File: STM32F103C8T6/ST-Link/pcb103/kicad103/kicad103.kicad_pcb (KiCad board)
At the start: 4 copper layers, 28 parts, among them IC1 LD1117DT33TR, J1 0480372200, J2 Conn_01x02_Socket, J3 Conn_02x05_Odd_Even, J4 Conn_01x03_Pin, J5 Conn_01x16_Pin, J6 Conn_01x16_Pin, J7 Conn_01x04_Pin, J8 Conn_01x05_Socket, U1 STM32F103C8T6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

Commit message: SWD 220R
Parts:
- added R6: 220, Resistor_SMD:R_1206_3216Metric, F.Cu at (233.1, 87.4)
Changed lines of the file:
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@@
+    )
+  )
+  (footprint "Resistor_SMD:R_1206_3216Metric" (layer "F.Cu")
+    (at 233.1375 87.4)
+    (descr "Resistor SMD 1206 (3216 Metric), square (rectangular) end terminal, IPC_7351 nominal, (Body size source: IPC-SM-782 page 72, https://www.pcb-3d.com/wordpress/wp-content/uploads/ipc-sm-782a_amendment_1_and_2.pdf), generated with kicad-footprint-generator")
+    (tags "resistor")
+    (property "Sheetfile" "kicad103.kicad_sch")
+    (property "Sheetname" "")
+    (property "ki_description" "Resistor")
+    (property "ki_keywords" "R res resistor")
+    (attr smd)
+    (fp_text reference "R6" (at 0 -1.82) (layer "F.SilkS")
+        (effects (font (size 1 1) (thickness 0.15)))
+    )
+    (fp_text value "220" (at 0 1.82) (layer "F.Fab")
+        (effects (font (size 1 1) (thickness 0.15)))
+    )
+    (fp_text user "${REFERENCE}" (at 0 0) (layer "F.Fab")
+        (effects (font (size 0.8 0.8) (thickness 0.12)))
+    )
+    (fp_line (start -0.727064 -0.91) (end 0.727064 -0.91)
+      (stroke (width 0.12) (type solid)) (layer "F.SilkS"))
+    (fp_line (start -0.727064 0.91) (end 0.727064 0.91)
+      (stroke (width 0.12) (type solid)) (layer "F.SilkS"))
+    (fp_line (start -2.28 -1.12) (end 2.28 -1.12)
+      (stroke (width 0.05) (type solid)) (layer "F.CrtYd"))
+    (fp_line (start -2.28 1.12) (end -2.28 -1.12)
+      (stroke (width 0.05) (type solid)) (layer "F.CrtYd"))
+    (fp_line (start 2.28 -1.12) (end 2.28 1.12)
+      (stroke (width 0.05) (type solid)) (layer "F.CrtYd"))
+    (fp_line (start 2.28 1.12) (end -2.28 1.12)
+      (stroke (width 0.05) (type solid)) (layer "F.CrtYd"))
+    (fp_line (start -1.6 -0.8) (end 1.6 -0.8)
+      (stroke (width 0.1) (type solid)) (layer "F.Fab"))
+    (fp_line (start -1.6 0.8) (end -1.6 -0.8)
+      (stroke (width 0.1) (type solid)) (layer "F.Fab"))
+    (fp_line (start 1.6 -0.8) (end 1.6 0.8)
+      (stroke (width 0.1) (type solid)) (layer "F.Fab"))
+    (fp_line (start 1.6 0.8) (end -1.6 0.8)
+      (stroke (width 0.1) (type solid)) (layer "F.Fab"))
+    (pad "1" smd roundrect (at -1.4625 0) (size 1.125 1.75) (layers "F.Cu" "F.Paste" "F.Mask") (roundrect_rratio 0.222222)
+      (net 22 "PB14") (pintype "passive"))
+    (pad "2" smd roundrect (at 1.4625 0) (size 1.125 1.75) (layers "F.Cu" "F.Paste" "F.Mask") (roundrect_rratio 0.222222)
+      (net 24 "PB12") (pintype "passive"))
+    (model "${KICAD6_3DMODEL_DIR}/Resistor_SMD.3dshapes/R_1206_3216Metric.wrl"
+      (offset (xyz 0 0 0))
+      (scale (xyz 1 1 1))
+      (rotate (xyz 0 0 0))
     )
   )

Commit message: Mounting holes
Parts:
- removed J4: Conn_01x03_Pin, Connector_PinHeader_2.54mm:PinHeader_1x03_P2.54mm_Vertical
- removed J6: Conn_01x16_Pin, Connector_PinHeader_2.54mm:PinHeader_1x16_P2.54mm_Vertical
- added H1: MountingHole_Pad, MountingHole:MountingHole_4.3mm_M4_Pad_Via, F.Cu at (243.2, 49.4)
- added H2: MountingHole_Pad, MountingHole:MountingHole_4.3mm_M4_Pad_Via, F.Cu at (243.2, 59.6)
- added H3: MountingHole_Pad, MountingHole:MountingHole_4.3mm_M4_Pad_Via, F.Cu at (243.2, 69.7)
- added H4: MountingHole_Pad, MountingHole:MountingHole_4.3mm_M4_Pad_Via, F.Cu at (243.2, 79.9)
- added J9: Conn_01x17_Pin, Connector_PinHeader_2.54mm:PinHeader_1x17_P2.54mm_Vertical, F.Cu at (235.8, 46.7)
- moved R2 31.8 mm to (183.5, 51.2)
- moved R1 31.8 mm to (183.5, 48.2)
- moved R5 31.8 mm to (144.4, 75.5)
- moved C5 31.8 mm to (149.4, 51.4)
- moved C6 31.8 mm to (149.4, 54.8)
- moved D2 31.8 mm to (193.8, 62.0)
- moved J3 31.8 mm to (147.0, 69.8)
- moved R4 31.8 mm to (165.1, 59.3)
- moved R6 31.8 mm to (201.7, 83.0)
- moved C1 31.8 mm to (203.4, 52.9)
- moved C2 31.8 mm to (202.8, 56.1)
- moved C3 31.8 mm to (149.4, 44.7)
- moved C4 31.8 mm to (149.4, 48.1)
- moved C7 31.8 mm to (149.4, 58.1)
- moved C8 31.8 mm to (156.0, 69.8)
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
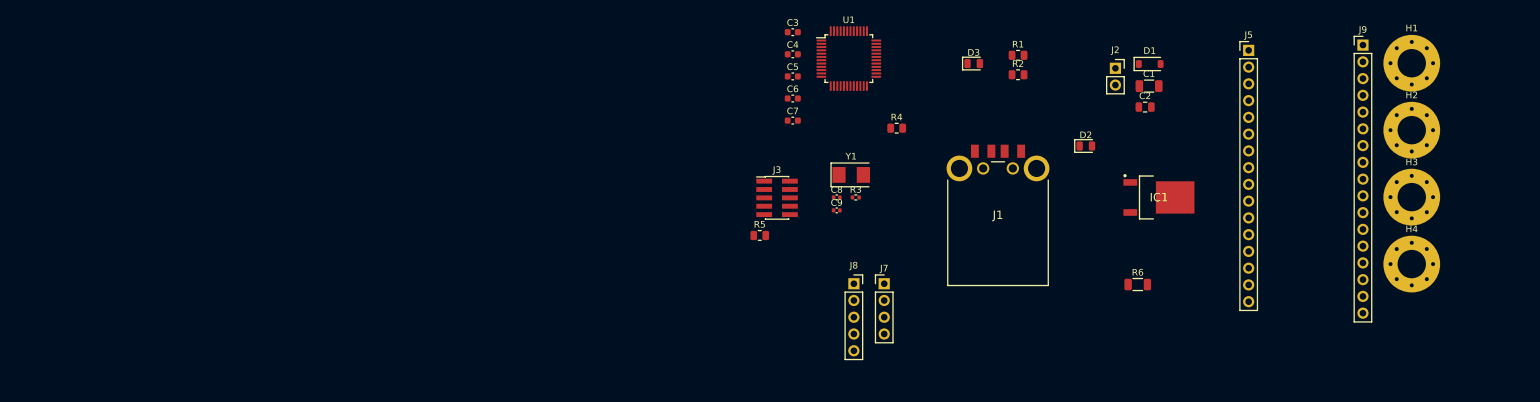
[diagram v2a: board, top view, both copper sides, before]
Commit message: Fix power lines
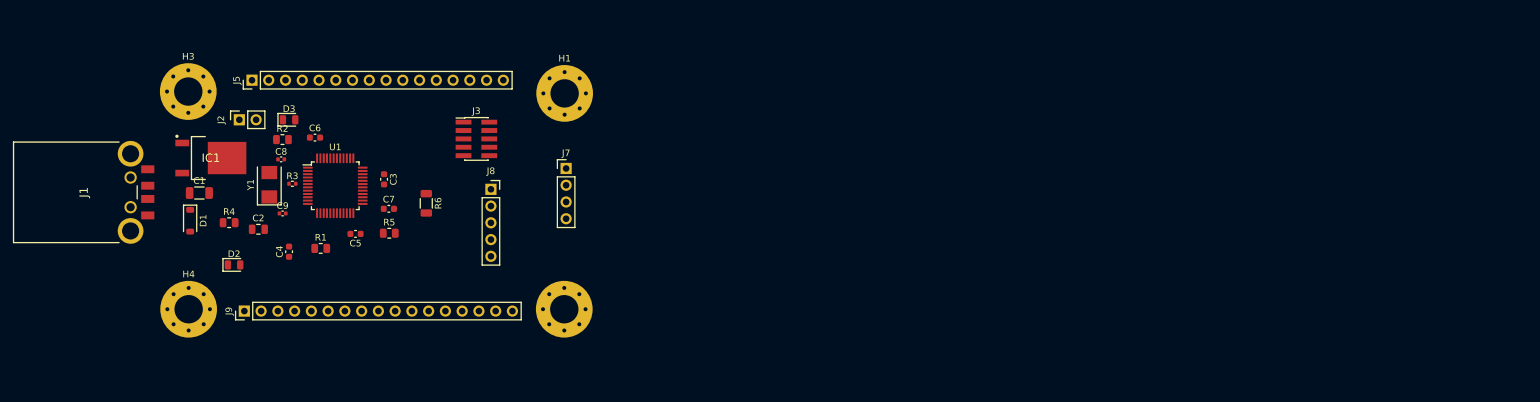
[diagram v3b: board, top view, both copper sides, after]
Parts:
- moved H3 186.2 mm to (57.7, 53.7)
- moved H4 185.6 mm to (57.8, 86.7)
- moved J9 174.3 mm to (66.2, 87.0), turned to 90 degrees
- moved J5 151.2 mm to (67.4, 52.0), turned to 90 degrees
- moved D1 147.4 mm to (58.0, 73.3), turned to -90 degrees
- moved C1 144.9 mm to (59.4, 69.1)
- moved IC1 143.8 mm to (61.1, 63.8)
- moved J1 139.1 mm to (41.4, 69.0), turned to -90 degrees
- moved C2 135.7 mm to (68.3, 74.6)
- moved J2 133.0 mm to (65.5, 58.0), turned to 90 degrees
- moved H2 131.3 mm to (114.7, 86.7)
- moved D2 130.4 mm to (64.7, 80.0)
- moved H1 128.5 mm to (114.8, 54.0)
- moved R2 111.9 mm to (72.0, 61.0)
- moved R1 109.7 mm to (77.8, 77.5)
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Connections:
- net +5V renamed Net-(D1-A)
- C2 pad 1: /3.3V -> +3.3V
- D2 pad 1: +3.3V -> Net-(D2-K)
- D2 pad 2: /3.3V -> +3.3V
- IC1 pad 4: /3.3V -> +3.3V
- R1 pad 1: +3.3V -> Net-(D2-K)
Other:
- rule pad_to_mask_clearance: 0 -> 0.038

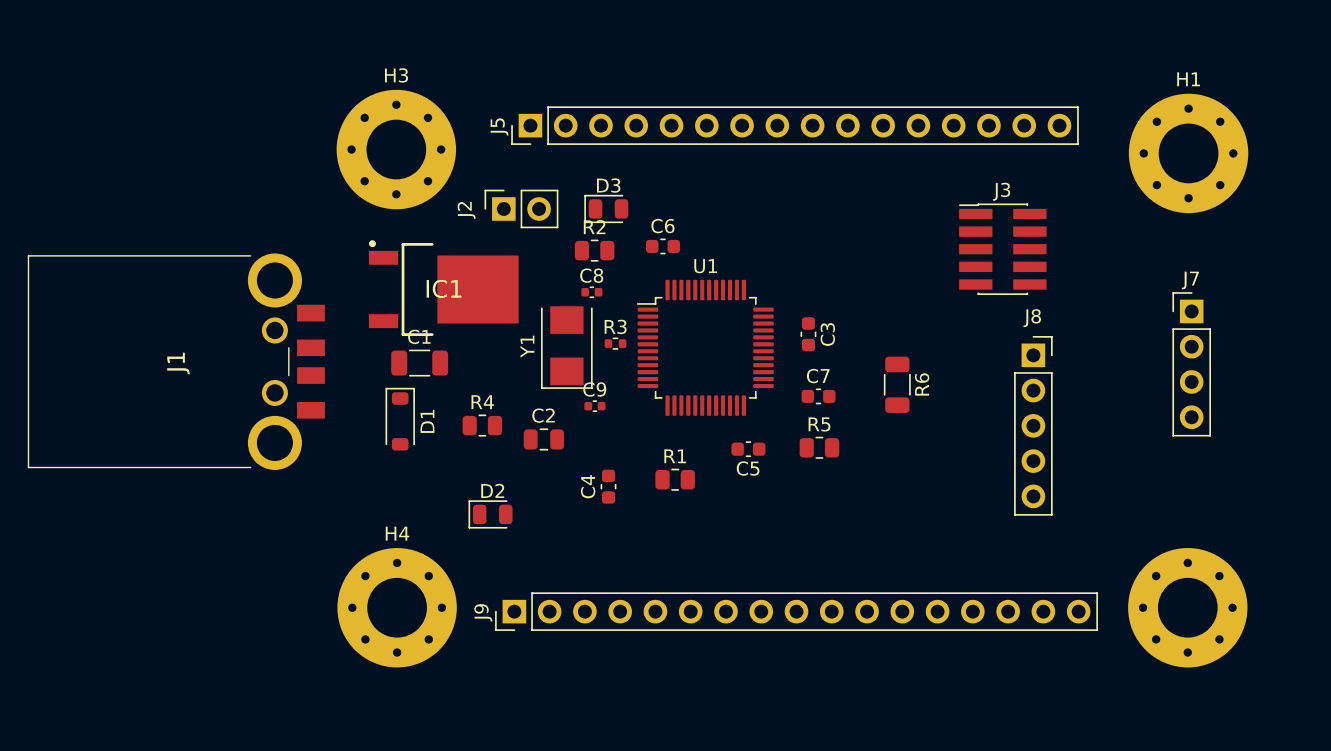
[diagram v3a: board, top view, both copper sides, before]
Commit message: USB differential pair
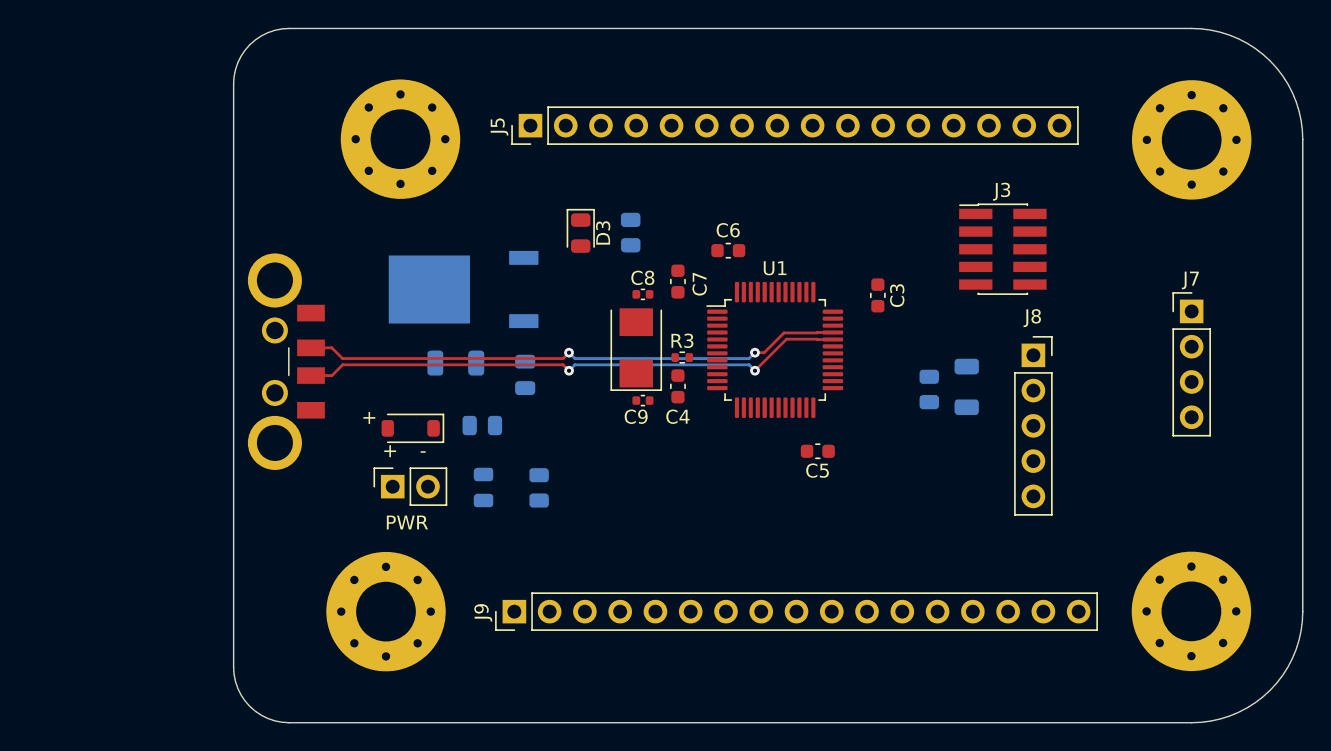
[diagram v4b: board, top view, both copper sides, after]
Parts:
- C1, C2, D2, IC1, R1, R2, R4, R5, R6: moved to B.Cu
- moved J2 21.5 mm to (57.5, 78.0)
- moved C7 13.1 mm to (78.0, 63.2), turned to 90 degrees
- moved R1 9.82 mm to (68.0, 78.1), turned to 90 degrees
- moved R5 8.96 mm to (96.1, 71.0), turned to 90 degrees
- moved C4 8.79 mm to (78.0, 70.8), turned to -90 degrees
- moved C3 5.73 mm to (92.4, 64.2)
- moved C5 5.00 mm to (88.1, 75.5)
- moved R6 5.00 mm to (98.8, 70.8)
- moved U1 5.00 mm to (85.0, 68.2)
- moved Y1 5.00 mm to (75.0, 68.0)
- moved R3 4.91 mm to (78.3, 68.7)
- moved C2 4.84 mm to (67.0, 70.0), turned to -90 degrees
- moved C6 4.71 mm to (81.6, 61.0)
- moved C8 3.68 mm to (75.5, 64.2), turned to 180 degrees
- moved C9 3.48 mm to (75.5, 71.8), turned to 180 degrees
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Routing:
- net /USB_D-: track 0.00 -> 39.4 mm, vias 0 -> 2
- net /USB_D+: track 0.00 -> 39.0 mm, vias 0 -> 2
- added copper zone on In2.Cu, net +3.3V
- added copper zone on In1.Cu, net GND
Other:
- board outline added: 77 x 50 mm
- board text added: "+"
- board text added: "-"
- board text added: "PWR"

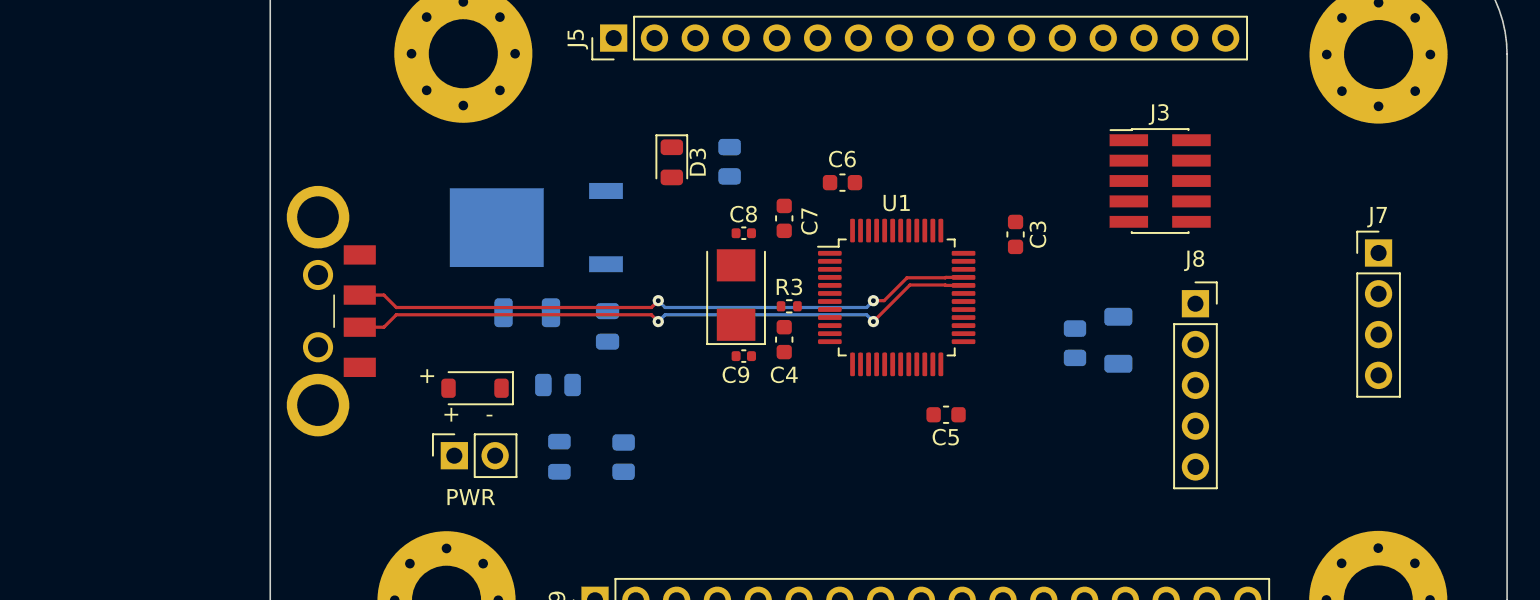
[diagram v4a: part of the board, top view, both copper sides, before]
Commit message: Connect Debug
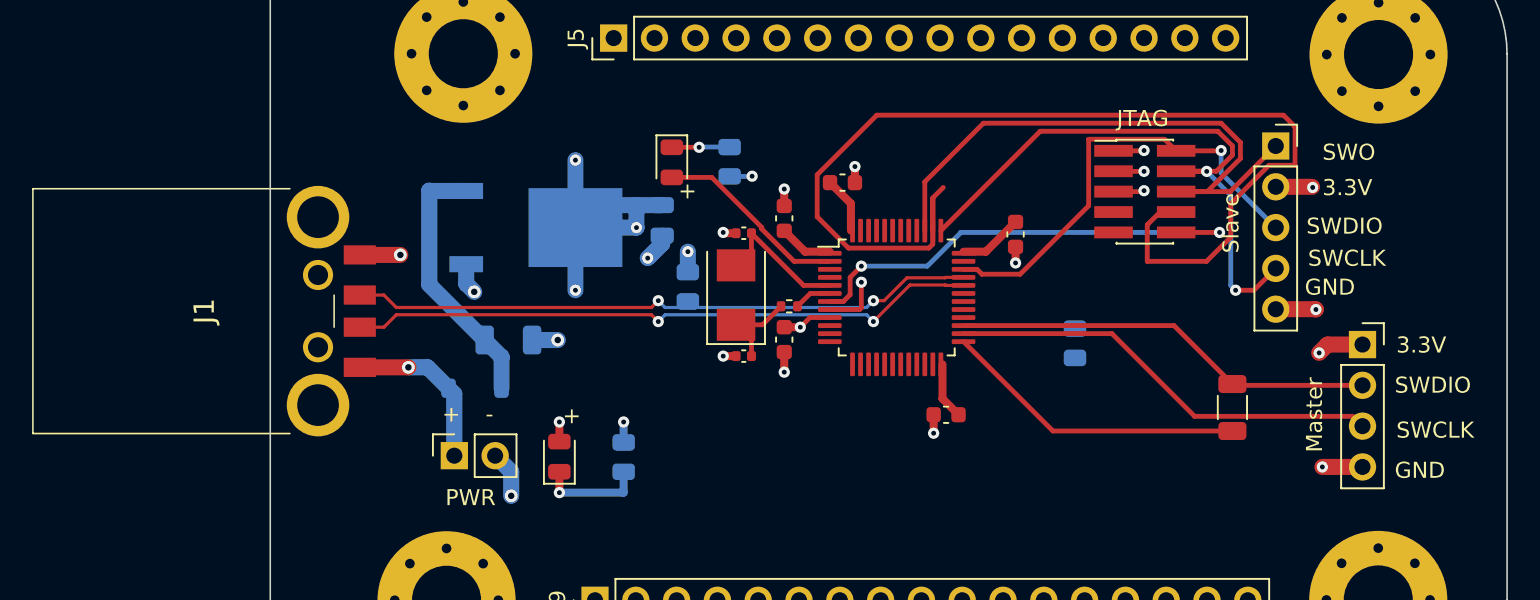
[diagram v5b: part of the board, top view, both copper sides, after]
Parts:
- D1: moved to B.Cu
- D2, R6: moved to F.Cu
- J7: footprint Connector_PinHeader_2.54mm:PinHeader_1x04_P2.54mm_Vertical -> Connector_PinSocket_2.54mm:PinSocket_1x04_P2.54mm_Vertical
- moved J8 11.0 mm to (108.6, 58.7)
- moved R4 10.1 mm to (72.0, 67.5), turned to -90 degrees
- moved R6 8.24 mm to (105.9, 75.0)
- moved C2 7.42 mm to (70.4, 63.4)
- moved J7 5.79 mm to (114.0, 71.1)
- moved C1 2.07 mm to (60.8, 70.8), turned to 0 degrees
- moved J3 1.16 mm to (100.5, 61.6)
- turned IC1 to 0 degrees
- turned R2 to -90 degrees
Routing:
- net PA15: track 0.00 -> 67.8 mm
- net +3.3V: track 0.00 -> 46.4 mm, vias 0 -> 9
- net PA14: track 0.00 -> 38.7 mm, vias 0 -> 2
- net PB3: track 0.00 -> 37.9 mm
- net GND: track 0.00 -> 33.2 mm, vias 0 -> 19
- net Net-(J3-Pin_10): track 0.00 -> 29.5 mm, vias 0 -> 2
- net PA13: track 0.00 -> 28.6 mm, vias 0 -> 1
- net PB13: track 0.00 -> 27.2 mm
- net PB14: track 0.00 -> 26.5 mm
- net PB12: track 0.00 -> 19.0 mm
- net Net-(D1-K): track 0.00 -> 16.5 mm
- net PC13: track 0.00 -> 12.1 mm
- net Net-(D1-A): track 0.00 -> 10.4 mm, vias 0 -> 1
- net Net-(U1-PD0): track 0.00 -> 8.62 mm
- net Net-(D2-K): track 0.00 -> 6.60 mm, vias 0 -> 1
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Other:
- board text added: "3.3V"
- board text added: "GND"
- board text added: "JTAG"
- board text added: "Master"
- board text added: "SWCLK"
- board text added: "SWDIO"
- board text added: "SWO"
- board text added: "Slave"

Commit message: J9
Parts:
- moved H4 0.74 mm to (57.7, 87.0)
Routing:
- net PC15: track 0.00 -> 72.8 mm, vias 0 -> 1
- net PC13: track 12.1 -> 79.3 mm
- net PC14: track 0.00 -> 38.6 mm, vias 0 -> 1
- net PA0: track 0.00 -> 24.7 mm
- net PA1: track 0.00 -> 24.1 mm, vias 0 -> 1
- net PA15: track 67.8 -> 91.6 mm, vias 0 -> 4
- net PA14: track 38.7 -> 61.9 mm
- net PA10: track 0.00 -> 22.5 mm, vias 0 -> 2
- net PA13: track 28.6 -> 49.9 mm, vias 1 -> 3
- net PA8: track 0.00 -> 21.1 mm
- net PA9: track 0.00 -> 20.9 mm, vias 0 -> 2
- net PA2: track 0.00 -> 20.1 mm
- net PA3: track 0.00 -> 18.6 mm
- net PA4: track 0.00 -> 17.3 mm
- net PA5: track 0.00 -> 16.5 mm
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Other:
- outline, holes or cut-outs redrawn
- board text added: "1"

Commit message: Connect all
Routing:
- net PB10: track 0.00 -> 128.0 mm, vias 0 -> 2
- net PB1: track 0.00 -> 124.3 mm, vias 0 -> 3
- net PB2: track 0.00 -> 122.5 mm, vias 0 -> 3
- net PB15: track 0.00 -> 122.3 mm, vias 0 -> 5
- net PB0: track 0.00 -> 115.9 mm, vias 0 -> 4
- net PB12: track 19.0 -> 117.3 mm, vias 0 -> 1
- net PB14: track 26.5 -> 98.2 mm, vias 0 -> 2
- net PB11: track 0.00 -> 65.7 mm, vias 0 -> 6
- net PB13: track 27.2 -> 88.4 mm, vias 0 -> 1
- net Net-(U1-BOOT0): track 0.00 -> 28.1 mm, vias 0 -> 1
- net PB4: track 0.00 -> 17.5 mm, vias 0 -> 2
- net PB5: track 0.00 -> 15.5 mm, vias 0 -> 2
- net PB3: track 37.9 -> 52.3 mm, vias 0 -> 2
- net PB6: track 0.00 -> 14.1 mm, vias 0 -> 2
- net PB7: track 0.00 -> 13.2 mm, vias 0 -> 2
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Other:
- board size 77 x 50 mm -> 82 x 52 mm
